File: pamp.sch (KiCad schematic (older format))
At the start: 54 parts, among them U201 LM1875, U202 LM1875

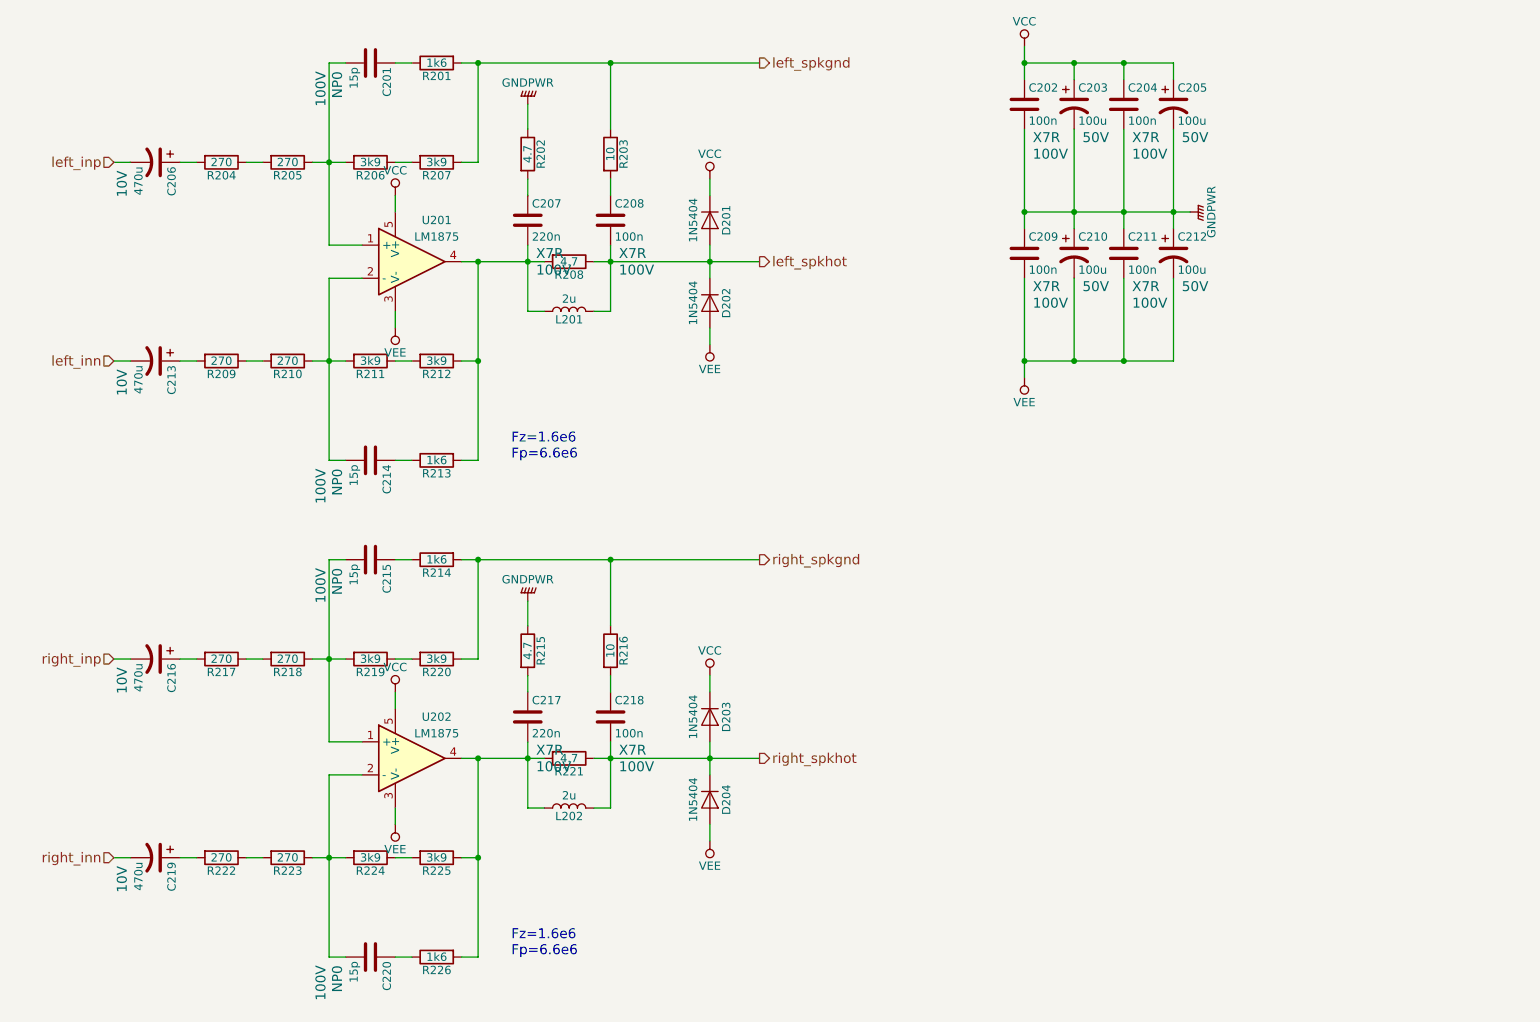
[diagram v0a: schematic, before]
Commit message: The board shall now support single channel only.
Signed-off-by: Nenad Radulovic <nenad.radulovic@seavus.com>
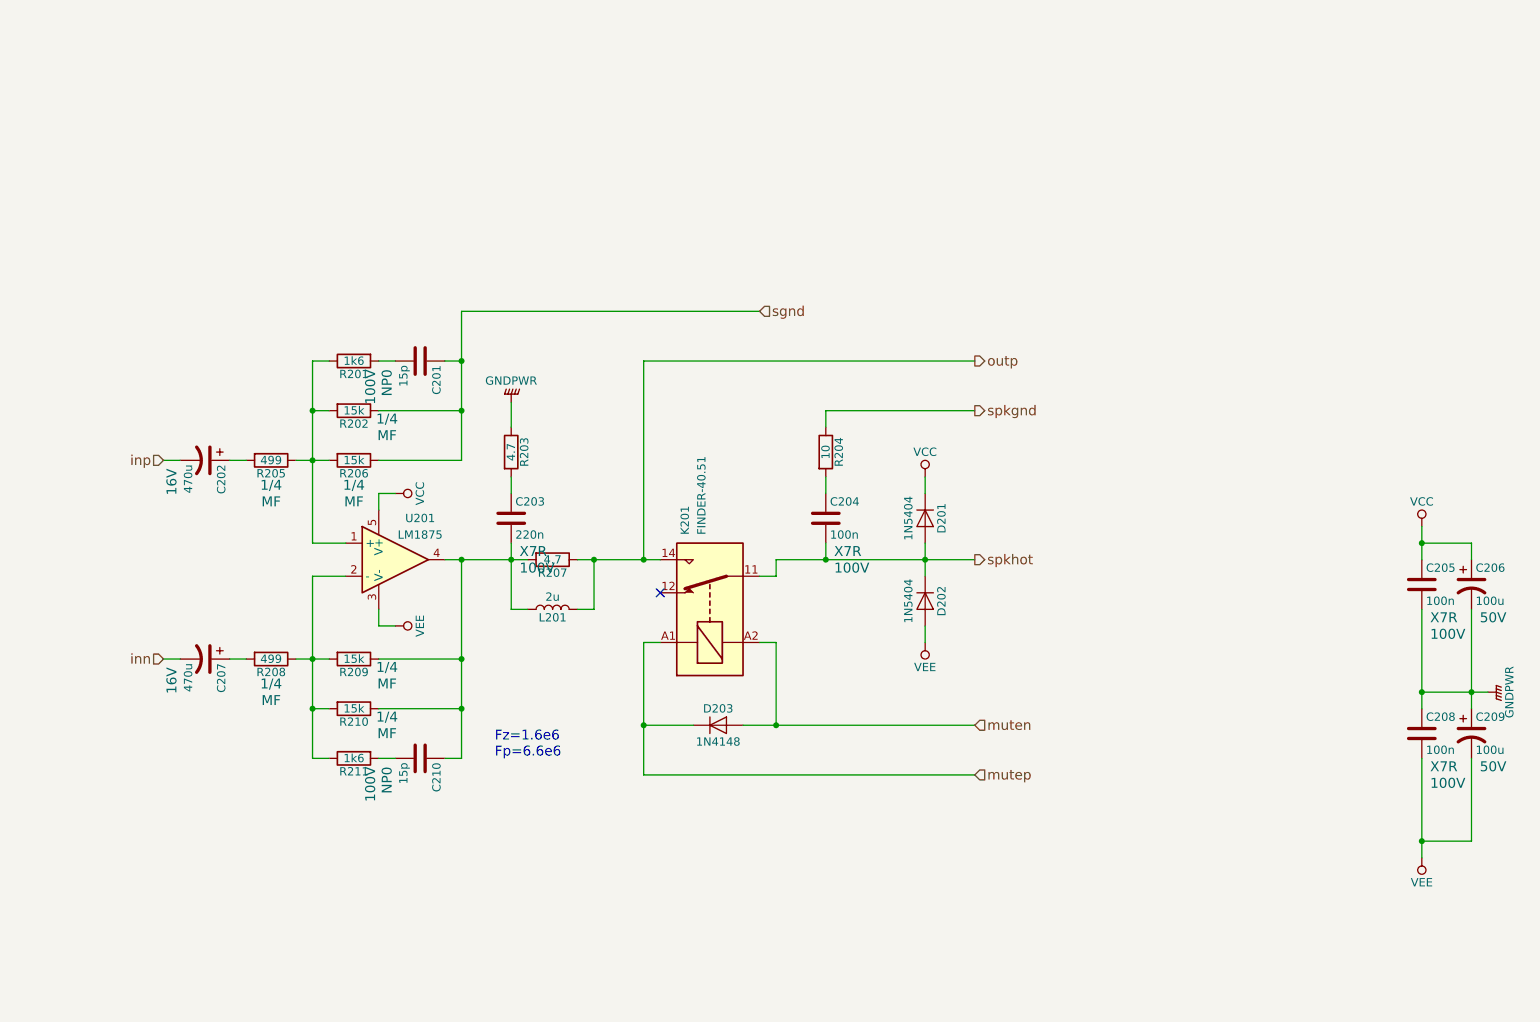
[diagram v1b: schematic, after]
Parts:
- removed C204, C211, C218: 100n, Capacitor_SMD:C_1206_3216Metric_Pad1.24x1.80mm_HandSolder, symbol C
- removed C205, C212: 100u, Capacitor_THT:CP_Radial_D8.0mm_P3.50mm, symbol CP1
- removed C215, C220: 15p, Capacitor_SMD:C_0805_2012Metric_Pad1.15x1.50mm_HandSolder, symbol C
- removed C216, C219: 470u, Capacitor_THT:CP_Radial_8.0mm_P3.50mm, symbol CP1
- removed C217: 220n, Capacitor_SMD:C_1206_3216Metric_Pad1.24x1.80mm_HandSolder, symbol C
- removed D203, D204: 1N5404, Diode_THT:D_DO-201AD_P12.70mm_Horizontal, symbol 1N5404
- removed L202: 2u, Choke_Axial_ThroughHole:Choke_Horizontal_RM15mm, symbol L
- removed R204, R217, R218, R222, R223: 270, Resistor_SMD:R_1206_3216Metric, symbol R
- removed R207, R211, R212, R219, R220, R224, R225: 3k9, Resistor_SMD:R_1206_3216Metric, symbol R
- removed R214, R226: 1k6, Resistor_SMD:R_1206_3216Metric, symbol R
- removed R215, R221: 4.7, Resistor_THT:R_Axial_DIN0411_L9.9mm_D3.6mm_P15.24mm_Horizontal, symbol R
- removed R216: 10, Resistor_THT:R_Axial_DIN0411_L9.9mm_D3.6mm_P15.24mm_Horizontal, symbol R
- removed U202: LM1875, TO_SOT_Packages_THT:TO-220-5_Pentawatt_Multiwatt-5_Vertical_StaggeredType1, symbol LM1875
- added D203: 1N4148, Diodes_THT:D_DO-35_SOD27_P7.62mm_Horizontal, symbol D
- added K201: FINDER-40.51, Relays_THT:Relay_SPDT_Finder_40.51, symbol FINDER-40.51
- added R202: 15k, Resistor_SMD:R_1206_3216Metric_Pad1.24x1.80mm_HandSolder, symbol R
- added R208: 499, Resistor_SMD:R_1206_3216Metric_Pad1.24x1.80mm_HandSolder, symbol R
- C202: renamed from C206; footprint Capacitor_THT:CP_Radial_8.0mm_P3.50mm -> Capacitor_THT:CP_Radial_D8.0mm_P3.50mm; Manufacturer Rybicon:10YXF470MEFC8X11.5 -> Rybicon:16YXJ470M8X11.5; Voltage 10V -> 16V
- C206: renamed from C203; Manufacturer Rybicon:50YXF100MEFC8X11.5 -> Rybicon:50YXJ100MT78X11.5; Vendor Farnell:1144634 -> Farnell:2346269
- C207: renamed from C213; footprint Capacitor_THT:CP_Radial_8.0mm_P3.50mm -> Capacitor_THT:CP_Radial_D8.0mm_P3.50mm; Manufacturer Rybicon:10YXF470MEFC8X11.5 -> Rybicon:16YXJ470M8X11.5; Voltage 10V -> 16V
- C209: renamed from C210; Manufacturer Rybicon:50YXF100MEFC8X11.5 -> Rybicon:50YXJ100MT78X11.5; Vendor Farnell:1144634 -> Farnell:2346269
- R201: footprint Resistor_SMD:R_1206_3216Metric -> Resistor_SMD:R_1206_3216Metric_Pad1.24x1.80mm_HandSolder
- R205: value 270 -> 499; footprint Resistor_SMD:R_1206_3216Metric -> Resistor_SMD:R_1206_3216Metric_Pad1.24x1.80mm_HandSolder; Manufacturer (none) -> PANASONIC:ERA8AEB4990V; Power (none) -> 1/4; Type (none) -> MF; Vendor (none) -> Farnell:2095153
- R206: value 3k9 -> 15k; footprint Resistor_SMD:R_1206_3216Metric -> Resistor_SMD:R_1206_3216Metric_Pad1.24x1.80mm_HandSolder; Manufacturer (none) -> PANASONIC:ERA8AEB153V; Power (none) -> 1/4; Type (none) -> MF; Vendor (none) -> Farnell:1717752
- R209, R210: value 270 -> 15k; footprint Resistor_SMD:R_1206_3216Metric -> Resistor_SMD:R_1206_3216Metric_Pad1.24x1.80mm_HandSolder; Manufacturer (none) -> PANASONIC:ERA8AEB153V; Power (none) -> 1/4; Type (none) -> MF; Vendor (none) -> Farnell:1717752
- R211: renamed from R213; footprint Resistor_SMD:R_1206_3216Metric -> Resistor_SMD:R_1206_3216Metric_Pad1.24x1.80mm_HandSolder
- renumbered C207 to C203, C208 to C204, C202 to C205, C209 to C208, C214 to C210, R202 to R203, R203 to R204, R208 to R207
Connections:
- net at R205.1, R206.2, U201.1 (+): now also R201.1, R202.2; no longer C201.2
- net at C203.2, L201.1, R207.2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: now also C210.1, R209.1, R210.1; no longer R211.2
- net at C202.1: now also R205.2
- net at R211.1: now also R209.2, R210.2, U201.2 (-), R208.1; no longer C210.1
- net sgnd: now reaches C201.1
- net sgnd: now also R206.1, R202.1; no longer R201.1
- net at C207.1: now also R208.2; no longer R209.2
- net left_inn renamed inn
- net left_inp renamed inp
- net left_spkgnd: no longer names the net of R201.2
- net left_spkgnd: now also C201.2; no longer R204.1
- net left_spkhot renamed spkhot
- net spkhot: now also K201.11; no longer L201.2, R207.1
- new net: C210.2, R211.2
- new net muten: D203.2 (A), K201.A2
- new net mutep: D203.1 (K), K201.A1
- new net outp: K201.14, L201.2, R207.1
- new net spkgnd: R204.1
- no-connect marks 0 -> 1
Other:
- moved on the sheet: C201, C202, C203, C204, C205, C206, C207, C208, C209, C210, D201, D202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

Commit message: Switched to Kicad 5.0
Signed-off-by: Nenad Radulovic <nenad.b.radulovic@gmail.com>
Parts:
- removed C201: 15p, Capacitor_SMD:C_0805_2012Metric_Pad1.15x1.50mm_HandSolder, symbol C
- removed C204: 100n, Capacitor_SMD:C_1206_3216Metric_Pad1.24x1.80mm_HandSolder, symbol C
- removed D203: 1N4148, Diodes_THT:D_DO-35_SOD27_P7.62mm_Horizontal, symbol D
- removed K201: FINDER-40.51, Relays_THT:Relay_SPDT_Finder_40.51, symbol FINDER-40.51
- removed R201: 1k6, Resistor_SMD:R_1206_3216Metric_Pad1.24x1.80mm_HandSolder, symbol R
- removed R202, R210: 15k, Resistor_SMD:R_1206_3216Metric_Pad1.24x1.80mm_HandSolder, symbol R
- removed R204: 10, Resistor_THT:R_Axial_DIN0411_L9.9mm_D3.6mm_P15.24mm_Horizontal, symbol R
- removed R205: 499, Resistor_SMD:R_1206_3216Metric_Pad1.24x1.80mm_HandSolder, symbol R
- removed U201: LM1875, TO_SOT_Packages_THT:TO-220-5_Pentawatt_Multiwatt-5_Vertical_StaggeredType1, symbol LM1875
- added C1: 15p, Capacitor_THT:C_Disc_D3.4mm_W2.1mm_P2.50mm, symbol Device:C
- added R1: 1k6, Resistor_THT:R_Axial_DIN0207_L6.3mm_D2.5mm_P10.16mm_Horizontal, symbol Device:R
- added R3: 499, Resistor_THT:R_Axial_DIN0207_L6.3mm_D2.5mm_P10.16mm_Horizontal, symbol Device:R
- added U1: LM1875, Package_TO_SOT_THT:TO-220-5_P3.4x3.7mm_StaggerOdd_Lead3.8mm_Vertical, symbol Amplifier_Audio:LM1875
- C2: renamed from C202; symbol CP1 -> Device:CP1
- C3: renamed from C203; footprint Capacitor_SMD:C_1206_3216Metric_Pad1.24x1.80mm_HandSolder -> Capacitor_THT:C_Rect_L7.0mm_W3.5mm_P5.00mm; symbol C -> Device:C
- C4: renamed from C205; footprint Capacitor_SMD:C_1206_3216Metric_Pad1.24x1.80mm_HandSolder -> Capacitor_THT:C_Rect_L7.0mm_W3.5mm_P5.00mm; symbol C -> Device:C
- C5: renamed from C206; symbol CP1 -> Device:CP1
- C6: renamed from C207; symbol CP1 -> Device:CP1
- C7: renamed from C210; footprint Capacitor_SMD:C_0805_2012Metric_Pad1.15x1.50mm_HandSolder -> Capacitor_THT:C_Disc_D3.8mm_W2.6mm_P2.50mm; symbol C -> Device:C
- C8: renamed from C208; footprint Capacitor_SMD:C_1206_3216Metric_Pad1.24x1.80mm_HandSolder -> Capacitor_THT:C_Rect_L7.0mm_W3.5mm_P5.00mm; symbol C -> Device:C
- C9: renamed from C209; symbol CP1 -> Device:CP1
- D1: renamed from D201; symbol 1N5404 -> Diode:1N5404
- D2: renamed from D202; symbol 1N5404 -> Diode:1N5404
- L1: renamed from L201; footprint Choke_Axial_ThroughHole:Choke_Horizontal_RM15mm -> Inductor_THT:L_Axial_L12.0mm_D5.0mm_P15.24mm_Horizontal_Fastron_MISC; symbol L -> Device:L
- R2: renamed from R203; symbol R -> Device:R
- R4: renamed from R206; footprint Resistor_SMD:R_1206_3216Metric_Pad1.24x1.80mm_HandSolder -> Resistor_THT:R_Axial_DIN0207_L6.3mm_D2.5mm_P10.16mm_Horizontal; symbol R -> Device:R
- R5: renamed from R207; symbol R -> Device:R
- R6: renamed from R208; footprint Resistor_SMD:R_1206_3216Metric_Pad1.24x1.80mm_HandSolder -> Resistor_THT:R_Axial_DIN0207_L6.3mm_D2.5mm_P10.16mm_Horizontal; symbol R -> Device:R
- R7: renamed from R209; footprint Resistor_SMD:R_1206_3216Metric_Pad1.24x1.80mm_HandSolder -> Resistor_THT:R_Axial_DIN0207_L6.3mm_D2.5mm_P10.16mm_Horizontal; symbol R -> Device:R
- R8: renamed from R211; footprint Resistor_SMD:R_1206_3216Metric_Pad1.24x1.80mm_HandSolder -> Resistor_THT:R_Axial_DIN0207_L6.3mm_D2.5mm_P10.16mm_Horizontal; symbol R -> Device:R
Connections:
- net inn is gone; now on net sgnd: C6.2
- net outp is gone; now on net spkhot: L1.2, R5.1
- net VCC: now also U1.5 (V+)
- net VEE: now also U1.3 (V-)
- net sgnd: now also C1.1
- net spkhot: no longer D1.2 (A), D2.1 (K)
- net at R4.2: now also R1.1, R3.1, U1.1 (+)
- net at R6.1, R7.2, R8.1: now also U1.2 (-)
- net at C3.2, C7.1, L1.1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: now also D1.2 (A), D2.1 (K), U1.4
- net at C2.1: now also R3.2
- new net: C1.2, R1.2
- no-connect marks 1 -> 0
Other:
- moved on the sheet: C2, C3, C6, C7, D1, D2, L1, R2, R4, R5, R6, R7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
